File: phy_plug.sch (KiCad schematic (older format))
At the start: 18 parts, among them J6 RJ45, U1 KSZ8081

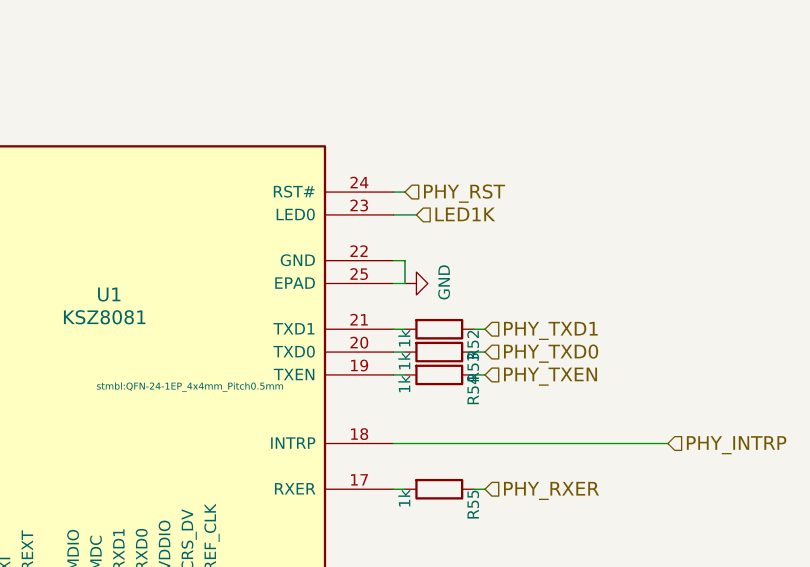
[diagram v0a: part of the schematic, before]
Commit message: Change to bigger housing
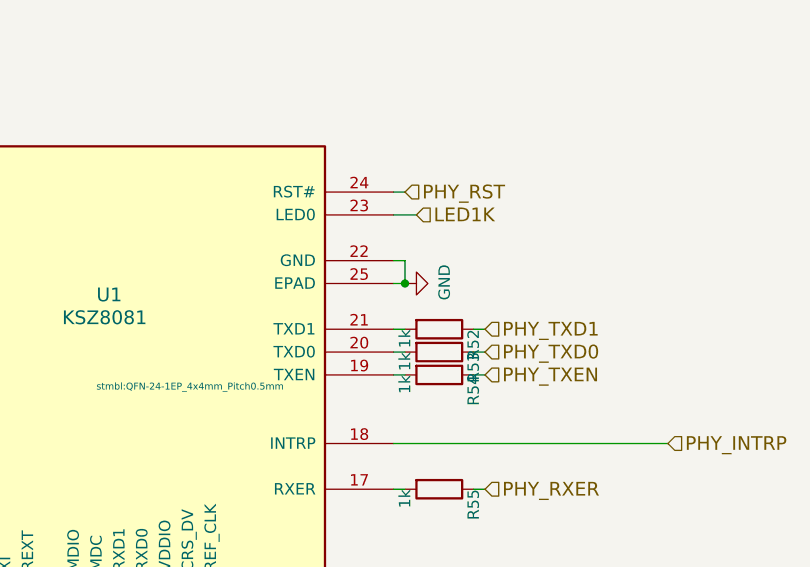
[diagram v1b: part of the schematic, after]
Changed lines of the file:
@@
-EESchema Schematic File Version 4
+EESchema Schematic File Version 5
+LIBS:powermetering-cache
 EELAYER 29 0
 EELAYER END
@@
 	1    0    0    -1
 $EndComp
+Connection ~ 4450 4100
 $EndSCHEMATC

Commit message: eth phy
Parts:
- removed J6: RJ45, symbol Connector:RJ45
- removed R55: 1k, stmbl:R_0603, symbol stmbl:R
- removed TR1: HX1333NL, powermetering:HX1333, symbol powermetering:HX1333NL
- added C72, C74: 100n, stmbl:C_0603, symbol stmbl:C
- added J6: HY951180A_RJ45, stmbl:HY951180A_RJ45, symbol stmbl:HY951180A_RJ45
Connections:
- net labels removed: PHY_RXER
- wire segments 48 -> 54
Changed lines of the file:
@@
 	0    -1   -1   0
-$EndComp
-Wire Wire Line
-	4400 5000 4450 5000
-Wire Wire Line
-	4750 5000 4800 5000
-Text HLabel 4800 5000 2    60   Input ~ 0
-PHY_RXER
-$Comp
-L stmbl:R R55
-U 1 1 57A9C5B8
-P 4600 5000
-F 0 "R55" H 4600 5150 50  0000 L CNN
-F 1 "1k" H 4600 4850 50  0000 L CNN
-F 2 "stmbl:R_0603" V 4530 5000 50  0001 C CNN
-F 3 "" H 4600 5000 50  0000 C CNN
-	1    4600 5000
-	0    1    1    0
 $EndComp
 $Comp
@@
 Wire Wire Line
 	2050 1100 2200 1100
+Connection ~ 4450 4100
 $Comp
-L Connector:RJ45 J6
-U 1 1 5DA066FB
-P 9450 4150
-F 0 "J6" H 9120 4154 50  0000 R CNN
-F 1 "RJ45" H 9120 4245 50  0000 R CNN
-F 2 "" V 9450 4175 50  0001 C CNN
-F 3 "~" V 9450 4175 50  0001 C CNN
-	1    9450 4150
-	-1   0    0    1
+L stmbl:HY951180A_RJ45 J6
+U 1 1 5DE1133E
+P 8000 4150
+F 0 "J6" H 7955 4897 60  0000 C CNN
+F 1 "HY951180A_RJ45" H 7955 4791 60  0000 C CNN
+F 2 "stmbl:HY951180A_RJ45" H 8000 4150 60  0001 C CNN
+F 3 "" H 8000 4150 60  0001 C CNN
+	1    8000 4150
+	1    0    0    -1
+$EndComp
+Text GLabel 7300 4000 0    60   Input ~ 0
+RX_N
+Text GLabel 7300 4200 0    60   Input ~ 0
+RX_P
+Text GLabel 7300 3650 0    60   Input ~ 0
+TX_N
+Text GLabel 7300 3850 0    60   Input ~ 0
+TX_P
+$Comp
+L stmbl:C C72
+U 1 1 5DE1368F
+P 6800 3750
+F 0 "C72" H 6850 3850 40  0000 L CNN
+F 1 "100n" H 6800 3650 40  0000 L CNN
+F 2 "stmbl:C_0603" H 6838 3600 30  0001 C CNN
+F 3 "" H 6800 3750 60  0000 C CNN
+	1    6800 3750
+	0    1    1    0
 $EndComp
 $Comp
-L powermetering:HX1333NL TR1
-U 1 1 5DA0E4FB
-P 7900 4200
-F 0 "TR1" H 7900 4742 50  0000 C CNN
-F 1 "HX1333NL" H 7900 4651 50  0000 C CNN
-F 2 "powermetering:HX1333" H 7900 3700 50  0001 C CNN
-F 3 "https://www.bourns.com/docs/Product-Datasheets/PT61017PEL.pdf" H 7200 4550 50  0001 C CNN
-	1    7900 4200
+L stmbl:C C74
+U 1 1 5DE14609
+P 6800 4100
+F 0 "C74" H 6850 4200 40  0000 L CNN
+F 1 "100n" H 6800 4000 40  0000 L CNN
+F 2 "stmbl:C_0603" H 6838 3950 30  0001 C CNN
+F 3 "" H 6800 4100 60  0000 C CNN
+	1    6800 4100
+	0    1    1    0
+$EndComp
+Wire Wire Line
+	7300 3650 7450 3650
+Wire Wire Line
+	7300 3850 7450 3850
+Wire Wire Line
+	6950 3750 7450 3750
+Wire Wire Line
+	6950 4100 7450 4100
+Wire Wire Line
+	7300 4000 7450 4000
+Wire Wire Line
+	7300 4200 7450 4200
+Wire Wire Line
+	6650 3750 6650 4100
+Connection ~ 6650 4100
+Wire Wire Line
+	6650 4100 6650 4300
+$Comp
+L power:GND #PWR0168
+U 1 1 5DE1B118
+P 6650 4300
+F 0 "#PWR0168" H 6650 4050 50  0001 C CNN
+F 1 "GND" H 6655 4127 50  0000 C CNN
+F 2 "" H 6650 4300 50  0000 C CNN
+F 3 "" H 6650 4300 50  0000 C CNN
+	1    6650 4300
 	1    0    0    -1
 $EndComp
-Connection ~ 4450 4100
 $EndSCHEMATC

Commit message: V2 hardware
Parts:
- added R? (x2): 1k, stmbl:R_0603, symbol stmbl:R
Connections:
- net LED1K is gone; now on an unnamed net: U1.23 (LED0)
- net GND: now also R?.2, R?.2
- net at J6.10 (GR_LED_K): now also R?.1
- net at J6.11 (Y_LED_K): now also R?.1
- net ETH_LED: now reaches J6.12 (Y_LED_A)
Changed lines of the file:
@@
 Wire Wire Line
 	3400 5700 3400 5850
-Text HLabel 4500 3800 2    60   Input ~ 0
-LED1K
-Wire Wire Line
-	4400 3800 4500 3800
 Text HLabel 4450 3700 2    60   Input ~ 0
 PHY_RST
@@
 	1    0    0    -1
 $EndComp
+Wire Wire Line
+	7300 4550 7450 4550
+$Comp
+L stmbl:R R?
+U 1 1 5D4500D6
+P 7150 4550
+F 0 "R?" H 7150 4700 50  0000 L CNN
+F 1 "1k" H 7150 4400 50  0000 L CNN
+F 2 "stmbl:R_0603" V 7080 4550 50  0001 C CNN
+F 3 "" H 7150 4550 50  0000 C CNN
+	1    7150 4550
+	0    1    1    0
+$EndComp
+$Comp
+L power:GND #PWR?
+U 1 1 5D4518CE
+P 6900 4550
+F 0 "#PWR?" H 6900 4300 50  0001 C CNN
+F 1 "GND" H 6905 4377 50  0000 C CNN
+F 2 "" H 6900 4550 50  0000 C CNN
+F 3 "" H 6900 4550 50  0000 C CNN
+	1    6900 4550
+	0    1    1    0
+$EndComp
+Wire Wire Line
+	6900 4550 7000 4550
+$Comp
+L stmbl:R R?
+U 1 1 5D454373
+P 7150 4800
+F 0 "R?" H 7150 4950 50  0000 L CNN
+F 1 "1k" H 7150 4650 50  0000 L CNN
+F 2 "stmbl:R_0603" V 7080 4800 50  0001 C CNN
+F 3 "" H 7150 4800 50  0000 C CNN
+	1    7150 4800
+	0    1    1    0
+$EndComp
+Wire Wire Line
+	7300 4800 7450 4800
+$Comp
+L power:GND #PWR?
+U 1 1 5D45437E
+P 6900 4800
+F 0 "#PWR?" H 6900 4550 50  0001 C CNN
+F 1 "GND" H 6905 4627 50  0000 C CNN
+F 2 "" H 6900 4800 50  0000 C CNN
+F 3 "" H 6900 4800 50  0000 C CNN
+	1    6900 4800
+	0    1    1    0
+$EndComp
+Wire Wire Line
+	6900 4800 7000 4800
+Wire Wire Line
+	5700 4450 5700 3800
+Wire Wire Line
+	4400 3800 5700 3800
+Wire Wire Line
+	5700 4450 7450 4450
+Wire Wire Line
+	7350 4700 7450 4700
+Text GLabel 7350 4700 0    50   Input ~ 0
+ETH_LED
 $EndSCHEMATC

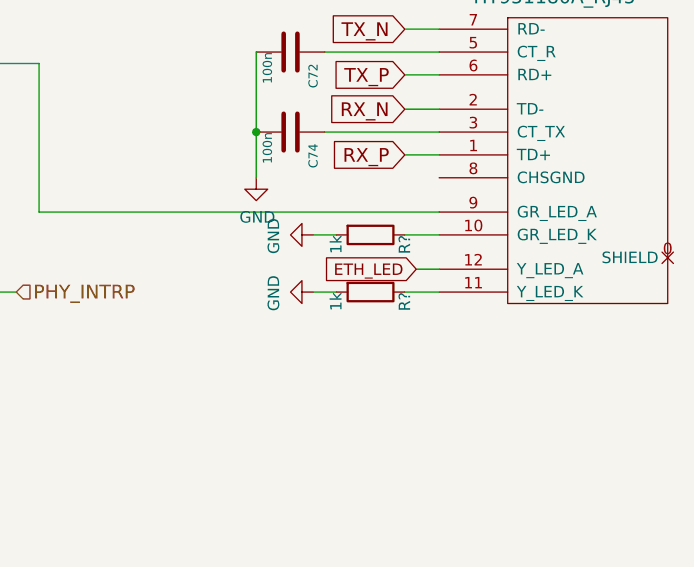
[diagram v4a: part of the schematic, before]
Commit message: swap phase order on current input
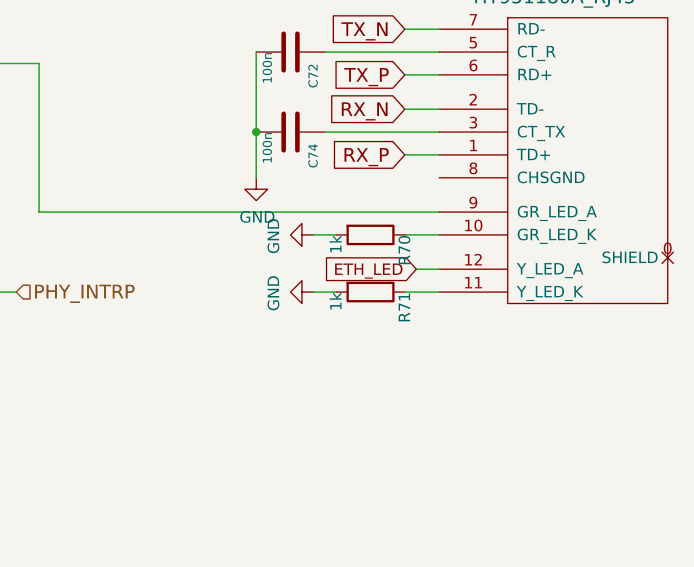
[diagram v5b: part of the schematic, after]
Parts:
- gave numbers to parts that had none: 2
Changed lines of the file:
@@
 	7300 4550 7450 4550
 $Comp
-L stmbl:R R?
+L stmbl:R R70
 U 1 1 5D4500D6
 P 7150 4550
-F 0 "R?" H 7150 4700 50  0000 L CNN
+F 0 "R70" H 7150 4700 50  0000 L CNN
 F 1 "1k" H 7150 4400 50  0000 L CNN
 F 2 "stmbl:R_0603" V 7080 4550 50  0001 C CNN
@@
 $EndComp
 $Comp
-L power:GND #PWR?
+L power:GND #PWR0193
 U 1 1 5D4518CE
 P 6900 4550
-F 0 "#PWR?" H 6900 4300 50  0001 C CNN
+F 0 "#PWR0193" H 6900 4300 50  0001 C CNN
 F 1 "GND" H 6905 4377 50  0000 C CNN
 F 2 "" H 6900 4550 50  0000 C CNN
@@
 	6900 4550 7000 4550
 $Comp
-L stmbl:R R?
+L stmbl:R R71
 U 1 1 5D454373
 P 7150 4800
-F 0 "R?" H 7150 4950 50  0000 L CNN
+F 0 "R71" H 7150 4950 50  0000 L CNN
 F 1 "1k" H 7150 4650 50  0000 L CNN
 F 2 "stmbl:R_0603" V 7080 4800 50  0001 C CNN
@@
 	7300 4800 7450 4800
 $Comp
-L power:GND #PWR?
+L power:GND #PWR0194
 U 1 1 5D45437E
 P 6900 4800
-F 0 "#PWR?" H 6900 4550 50  0001 C CNN
+F 0 "#PWR0194" H 6900 4550 50  0001 C CNN
 F 1 "GND" H 6905 4627 50  0000 C CNN
 F 2 "" H 6900 4800 50  0000 C CNN

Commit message: small production changes
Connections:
- net GND: now also J6.8 (CHSGND)
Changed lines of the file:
@@
 Text GLabel 7350 4700 0    50   Input ~ 0
 ETH_LED
+$Comp
+L power:GND #PWR0199
+U 1 1 5D2D4E66
+P 7350 4300
+F 0 "#PWR0199" H 7350 4050 50  0001 C CNN
+F 1 "GND" H 7355 4127 50  0000 C CNN
+F 2 "" H 7350 4300 50  0000 C CNN
+F 3 "" H 7350 4300 50  0000 C CNN
+	1    7350 4300
+	0    1    1    0
+$EndComp
+Wire Wire Line
+	7350 4300 7450 4300
 $EndSCHEMATC
